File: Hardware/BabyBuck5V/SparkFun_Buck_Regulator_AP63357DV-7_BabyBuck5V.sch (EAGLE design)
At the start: 20 parts, among them U1 AP63357

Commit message: Swap POP for UnPOP'd connector.
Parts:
- J1: device SparkFun-Connectors:CONN_041X04_NO_SILK -> SparkFun-Connectors:CONN_041X04_NO_SILK_NO_POP
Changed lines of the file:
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@@
 <part name="C5" library="SparkFun-Capacitors" deviceset="4.7UF" device="-0805-50V-(10%)" value="4.7uF"/>
 <part name="GND10" library="SparkFun-PowerSymbols" deviceset="GND" device=""/>
-<part name="J1" library="SparkFun-Connectors" deviceset="CONN_04" device="1X04_NO_SILK"/>
+<part name="J1" library="SparkFun-Connectors" deviceset="CONN_04" device="1X04_NO_SILK_NO_POP"/>
 </parts>
 <sheets>

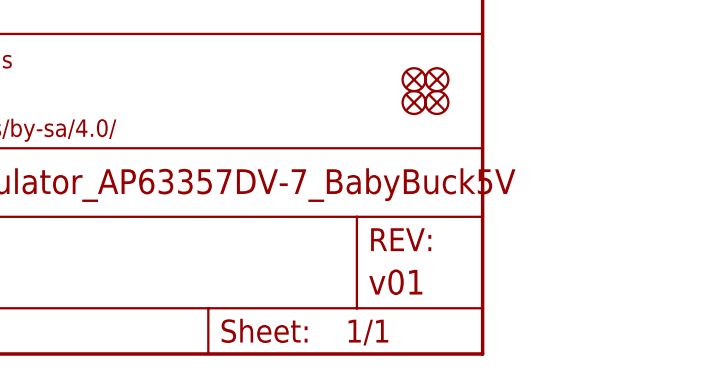
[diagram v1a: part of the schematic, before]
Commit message: Ready for v10 reds.
1x1 - Thicken silk border on U1
micro - Move fiducial to increase heat sink size
both - panelize
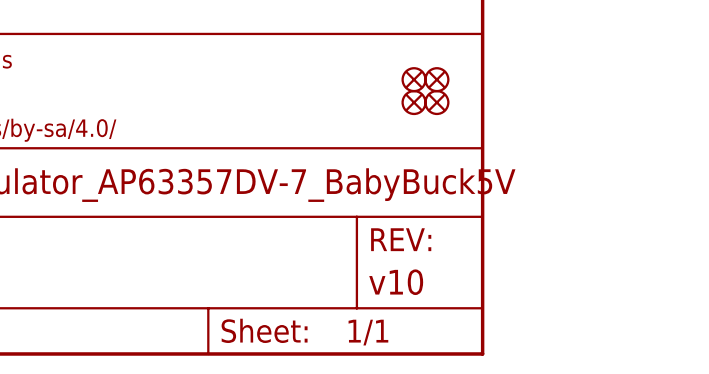
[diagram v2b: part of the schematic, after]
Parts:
- FRAME1: REV v01 -> v10
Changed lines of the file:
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@@
 <part name="FRAME1" library="SparkFun-Aesthetics" deviceset="FRAME-LEDGER" device="">
 <attribute name="DESIGNER" value="Alex Brudner"/>
-<attribute name="REV" value="v01"/>
+<attribute name="REV" value="v10"/>
 </part>
 <part name="FD3" library="SparkFun-Aesthetics" deviceset="FIDUCIAL" device="UFIDUCIAL"/>
